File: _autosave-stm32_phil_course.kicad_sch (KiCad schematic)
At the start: 16 parts

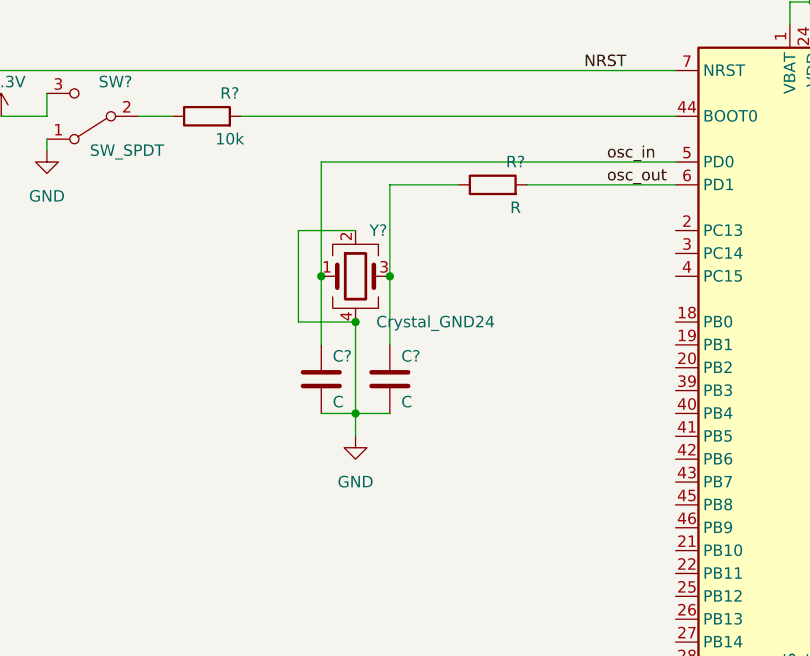
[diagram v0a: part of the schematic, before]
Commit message: add 2 pins oscillator to schematic
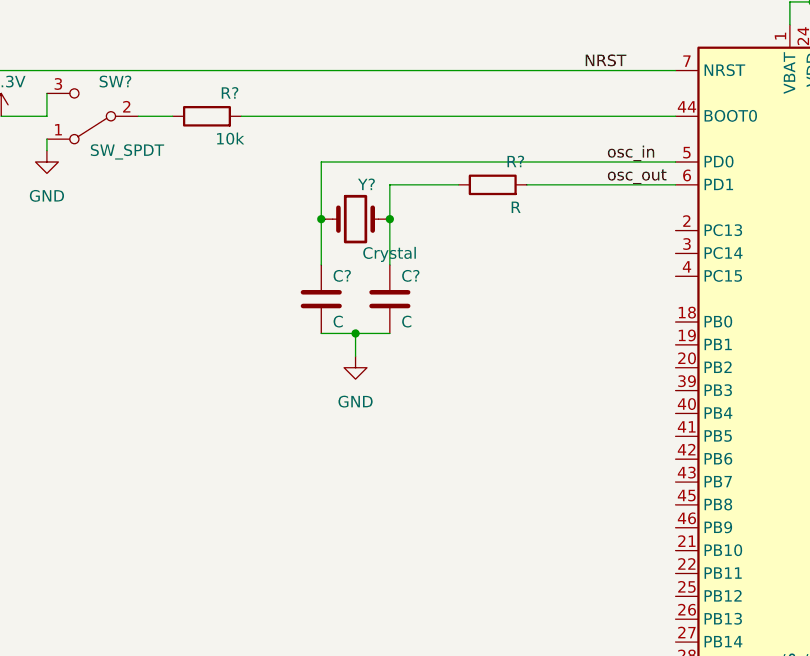
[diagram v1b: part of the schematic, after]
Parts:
- removed Y?: Crystal_GND24, symbol Device:Crystal_GND24
- added Y?: Crystal, symbol Device:Crystal
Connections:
- net osc_in: now also Y?.1
- net at C?.1, R?.1: now also Y?.2
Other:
- moved on the sheet: C?
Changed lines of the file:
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@@
   (junction (at 110.49 41.91) (diameter 0) (color 0 0 0 0)
   )
+  (junction (at 90.17 77.47) (diameter 0) (color 0 0 0 0)
+  )
   (junction (at 152.4 34.29) (diameter 0) (color 0 0 0 0)
   )
   (junction (at 144.78 53.34) (diameter 0) (color 0 0 0 0)
   )
-  (junction (at 97.79 83.82) (diameter 0) (color 0 0 0 0)
+  (junction (at 97.79 77.47) (diameter 0) (color 0 0 0 0)
   )
   (junction (at 97.79 34.29) (diameter 0) (color 0 0 0 0)
@@
   (junction (at 194.31 34.29) (diameter 0) (color 0 0 0 0)
   )
-  (junction (at 90.17 83.82) (diameter 0) (color 0 0 0 0)
-  )
   (junction (at 110.49 34.29) (diameter 0) (color 0 0 0 0)
   )
@@
   (junction (at 147.32 134.62) (diameter 0) (color 0 0 0 0)
   )
-  (junction (at 93.98 88.9) (diameter 0) (color 0 0 0 0)
-  )
-  (junction (at 93.98 99.06) (diameter 0) (color 0 0 0 0)
+  (junction (at 93.98 90.17) (diameter 0) (color 0 0 0 0)
   )
   (junction (at 146.05 53.34) (diameter 0) (color 0 0 0 0)
@@
     (stroke (width 0) (type default) (color 0 0 0 0))
   )
-  (wire (pts (xy 97.79 73.66) (xy 97.79 83.82))
-    (stroke (width 0) (type default) (color 0 0 0 0))
-  )
   (wire (pts (xy 146.05 34.29) (xy 146.05 33.02))
     (stroke (width 0) (type default) (color 0 0 0 0))
@@
     (stroke (width 0) (type default) (color 0 0 0 0))
   )
-  (wire (pts (xy 90.17 83.82) (xy 90.17 91.44))
-    (stroke (width 0) (type default) (color 0 0 0 0))
-  )
-  (wire (pts (xy 93.98 88.9) (xy 93.98 99.06))
-    (stroke (width 0) (type default) (color 0 0 0 0))
-  )
-  (wire (pts (xy 87.63 78.74) (xy 87.63 88.9))
-    (stroke (width 0) (type default) (color 0 0 0 0))
-  )
   (wire (pts (xy 39.37 60.96) (xy 129.54 60.96))
     (stroke (width 0) (type default) (color 0 0 0 0))
@@
     (stroke (width 0) (type default) (color 0 0 0 0))
   )
-  (wire (pts (xy 97.79 99.06) (xy 93.98 99.06))
+  (wire (pts (xy 97.79 90.17) (xy 93.98 90.17))
+    (stroke (width 0) (type default) (color 0 0 0 0))
+  )
+  (wire (pts (xy 97.79 77.47) (xy 97.79 82.55))
     (stroke (width 0) (type default) (color 0 0 0 0))
   )
@@
     (stroke (width 0) (type default) (color 0 0 0 0))
   )
+  (wire (pts (xy 90.17 77.47) (xy 90.17 82.55))
+    (stroke (width 0) (type default) (color 0 0 0 0))
+  )
   (wire (pts (xy 149.86 53.34) (xy 149.86 55.88))
     (stroke (width 0) (type default) (color 0 0 0 0))
@@
     (stroke (width 0) (type default) (color 0 0 0 0))
   )
-  (wire (pts (xy 90.17 71.12) (xy 90.17 83.82))
-    (stroke (width 0) (type default) (color 0 0 0 0))
-  )
-  (wire (pts (xy 93.98 99.06) (xy 93.98 101.6))
+  (wire (pts (xy 90.17 71.12) (xy 90.17 77.47))
+    (stroke (width 0) (type default) (color 0 0 0 0))
+  )
+  (wire (pts (xy 93.98 90.17) (xy 93.98 92.71))
     (stroke (width 0) (type default) (color 0 0 0 0))
   )
@@
     (stroke (width 0) (type default) (color 0 0 0 0))
   )
-  (wire (pts (xy 93.98 78.74) (xy 87.63 78.74))
-    (stroke (width 0) (type default) (color 0 0 0 0))
-  )
   (wire (pts (xy 85.09 41.91) (xy 97.79 41.91))
     (stroke (width 0) (type default) (color 0 0 0 0))
   )
-  (wire (pts (xy 97.79 83.82) (xy 97.79 91.44))
+  (wire (pts (xy 97.79 73.66) (xy 97.79 77.47))
     (stroke (width 0) (type default) (color 0 0 0 0))
   )
@@
     (stroke (width 0) (type default) (color 0 0 0 0))
   )
-  (wire (pts (xy 87.63 88.9) (xy 93.98 88.9))
-    (stroke (width 0) (type default) (color 0 0 0 0))
-  )
-  (wire (pts (xy 90.17 99.06) (xy 93.98 99.06))
+  (wire (pts (xy 90.17 90.17) (xy 93.98 90.17))
     (stroke (width 0) (type default) (color 0 0 0 0))
   )
@@
     (pin "1")
   )
-  (symbol (lib_id "power:GND") (at 93.98 101.6 0) (unit 1)
-    (in_bom yes) (on_board yes) (fields_autoplaced)
-    (property "Reference" "#PWR?" (id 0) (at 93.98 107.95 0)
-      (effects (font (size 1.27 1.27)) hide)
-    )
-    (property "Value" "GND" (id 1) (at 93.98 106.68 0))
-    (property "Footprint" "" (id 2) (at 93.98 101.6 0)
-      (effects (font (size 1.27 1.27)) hide)
-    )
-    (property "Datasheet" "" (id 3) (at 93.98 101.6 0)
+  (symbol (lib_id "power:GND") (at 93.98 92.71 0) (unit 1)
+    (in_bom yes) (on_board yes) (fields_autoplaced)
+    (property "Reference" "#PWR?" (id 0) (at 93.98 99.06 0)
+      (effects (font (size 1.27 1.27)) hide)
+    )
+    (property "Value" "GND" (id 1) (at 93.98 97.79 0))
+    (property "Footprint" "" (id 2) (at 93.98 92.71 0)
+      (effects (font (size 1.27 1.27)) hide)
+    )
+    (property "Datasheet" "" (id 3) (at 93.98 92.71 0)
       (effects (font (size 1.27 1.27)) hide)
     )
@@
     (pin "1")
   )
+  (symbol (lib_id "Device:Crystal") (at 93.98 77.47 0) (unit 1)
+    (in_bom yes) (on_board yes)
+    (property "Reference" "Y?" (id 0) (at 95.25 73.66 0))
+    (property "Value" "Crystal" (id 1) (at 97.79 81.28 0))
+    (property "Footprint" "" (id 2) (at 93.98 77.47 0)
+      (effects (font (size 1.27 1.27)) hide)
+    )
+    (property "Datasheet" "~" (id 3) (at 93.98 77.47 0)
+      (effects (font (size 1.27 1.27)) hide)
+    )
+    (pin "1")
+    (pin "2")
+  )
   (symbol (lib_id "Device:C") (at 194.31 38.1 0) (unit 1)
     (in_bom yes) (on_board yes) (fields_autoplaced)
@@
     (pin "2")
   )
-  (symbol (lib_id "Device:C") (at 90.17 95.25 0) (unit 1)
+  (symbol (lib_id "Device:C") (at 90.17 86.36 0) (unit 1)
     (in_bom yes) (on_board yes)
-    (property "Reference" "C?" (id 0) (at 91.44 92.71 0)
-      (effects (font (size 1.27 1.27)) (justify left))
-    )
-    (property "Value" "C" (id 1) (at 91.44 97.79 0)
-      (effects (font (size 1.27 1.27)) (justify left))
-    )
-    (property "Footprint" "" (id 2) (at 91.1352 99.06 0)
-      (effects (font (size 1.27 1.27)) hide)
-    )
-    (property "Datasheet" "~" (id 3) (at 90.17 95.25 0)
+    (property "Reference" "C?" (id 0) (at 91.44 83.82 0)
+      (effects (font (size 1.27 1.27)) (justify left))
+    )
+    (property "Value" "C" (id 1) (at 91.44 88.9 0)
+      (effects (font (size 1.27 1.27)) (justify left))
+    )
+    (property "Footprint" "" (id 2) (at 91.1352 90.17 0)
+      (effects (font (size 1.27 1.27)) hide)
+    )
+    (property "Datasheet" "~" (id 3) (at 90.17 86.36 0)
       (effects (font (size 1.27 1.27)) hide)
     )
@@
     (pin "1")
   )
-  (symbol (lib_id "Device:C") (at 97.79 95.25 0) (unit 1)
+  (symbol (lib_id "Device:C") (at 97.79 86.36 0) (unit 1)
     (in_bom yes) (on_board yes)
-    (property "Reference" "C?" (id 0) (at 99.06 92.71 0)
-      (effects (font (size 1.27 1.27)) (justify left))
-    )
-    (property "Value" "C" (id 1) (at 99.06 97.79 0)
-      (effects (font (size 1.27 1.27)) (justify left))
-    )
-    (property "Footprint" "" (id 2) (at 98.7552 99.06 0)
-      (effects (font (size 1.27 1.27)) hide)
-    )
-    (property "Datasheet" "~" (id 3) (at 97.79 95.25 0)
-      (effects (font (size 1.27 1.27)) hide)
-    )
-    (pin "1")
-    (pin "2")
-  )
-  (symbol (lib_id "Device:Crystal_GND24") (at 93.98 83.82 0) (unit 1)
-    (in_bom yes) (on_board yes)
-    (property "Reference" "Y?" (id 0) (at 96.52 78.74 0))
-    (property "Value" "Crystal_GND24" (id 1) (at 102.87 88.9 0))
-    (property "Footprint" "" (id 2) (at 93.98 83.82 0)
-      (effects (font (size 1.27 1.27)) hide)
-    )
-    (property "Datasheet" "~" (id 3) (at 93.98 83.82 0)
-      (effects (font (size 1.27 1.27)) hide)
-    )
-    (pin "1")
-    (pin "2")
-    (pin "3")
-    (pin "4")
+    (property "Reference" "C?" (id 0) (at 99.06 83.82 0)
+      (effects (font (size 1.27 1.27)) (justify left))
+    )
+    (property "Value" "C" (id 1) (at 99.06 88.9 0)
+      (effects (font (size 1.27 1.27)) (justify left))
+    )
+    (property "Footprint" "" (id 2) (at 98.7552 90.17 0)
+      (effects (font (size 1.27 1.27)) hide)
+    )
+    (property "Datasheet" "~" (id 3) (at 97.79 86.36 0)
+      (effects (font (size 1.27 1.27)) hide)
+    )
+    (pin "1")
+    (pin "2")
   )
   (symbol (lib_id "Device:R") (at 77.47 66.04 90) (unit 1)
@@
       (reference "U?") (unit 1) (value "STM32F103C8T6") (footprint "Package_QFP:LQFP-48_7x7mm_P0.5mm")
     )
-    (path "/ac5b2370-b44d-46c3-8f04-430447004b96"
-      (reference "Y?") (unit 1) (value "Crystal_GND24") (footprint "")
-    )
-  )
+    (path "/590a19f0-2ba9-487e-92f9-66b7f62ad098"
+      (reference "Y?") (unit 1) (value "Crystal") (footprint "")
+    )
+  )
